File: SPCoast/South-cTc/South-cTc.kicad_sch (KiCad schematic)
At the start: 17 parts, among them SW783 783, SW795 795, SW799 799, U1 8, U2 9, U3 10

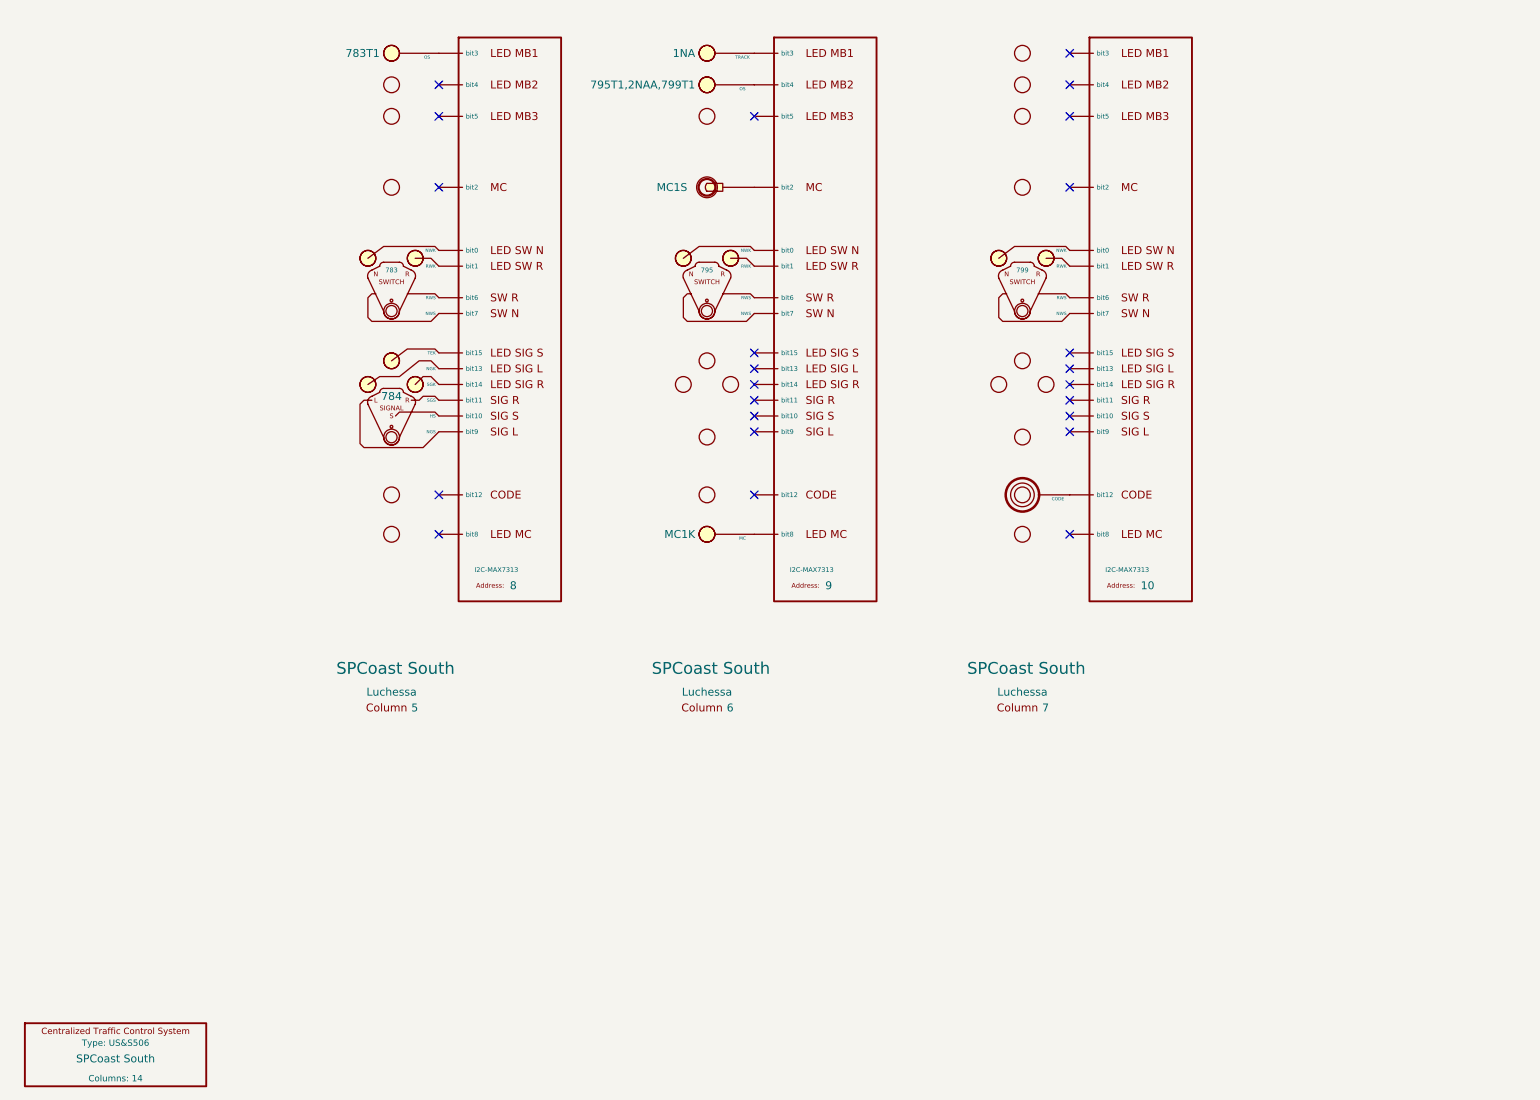
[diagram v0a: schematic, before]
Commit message: feat(kicad): restructure South-cTc into per-interlocking sheets with codelines
- Root sheet holds the CtcMachine; one hierarchical sheet per
  interlocking (Gilroy CalTrain, Gilroy Interchange, Luchessa,
  Christopher, Corporal, Sargent, Watsonville), each with a
  Codeline-VIRTUAL symbol carrying its Station.
- Luchessa sheet: columns 5-7 bind their appliances by column pins
  (membership from the netlist, not X alignment); appliances and drivers
  carry Role/Kind.
- Repair: root sheet UUID now matches the instance paths (kicad-cli
  exported zero nets before); .kicad_pro root filename case restored.
- Normalise Role/Kind values (MACHINE, COLUMN, APPLIANCE, IODRIVER;
  SWITCH_LEVER, SIGNAL_LEVER, LOCK_LEVER, LAMP, CODE, MAINTAINER_CALL),
  point stale PanelColumn_1/_2 copies back at the library symbol, and
  restore lamp IndicationTokens (783T1, 795T1,2NAA,799T1, 1NA, MC1K)
  lost to a library default.

Verified: kicad-cli netlist has 72 nets; ERC 0 violations; desk
playtest resolves every Luchessa appliance to one column and its
MAX7313 bits, matching examples/spcoast_ctc/IO-I2C.h.

Co-Authored-By: Claude Opus 5.5 (1M context) <noreply@anthropic.com>
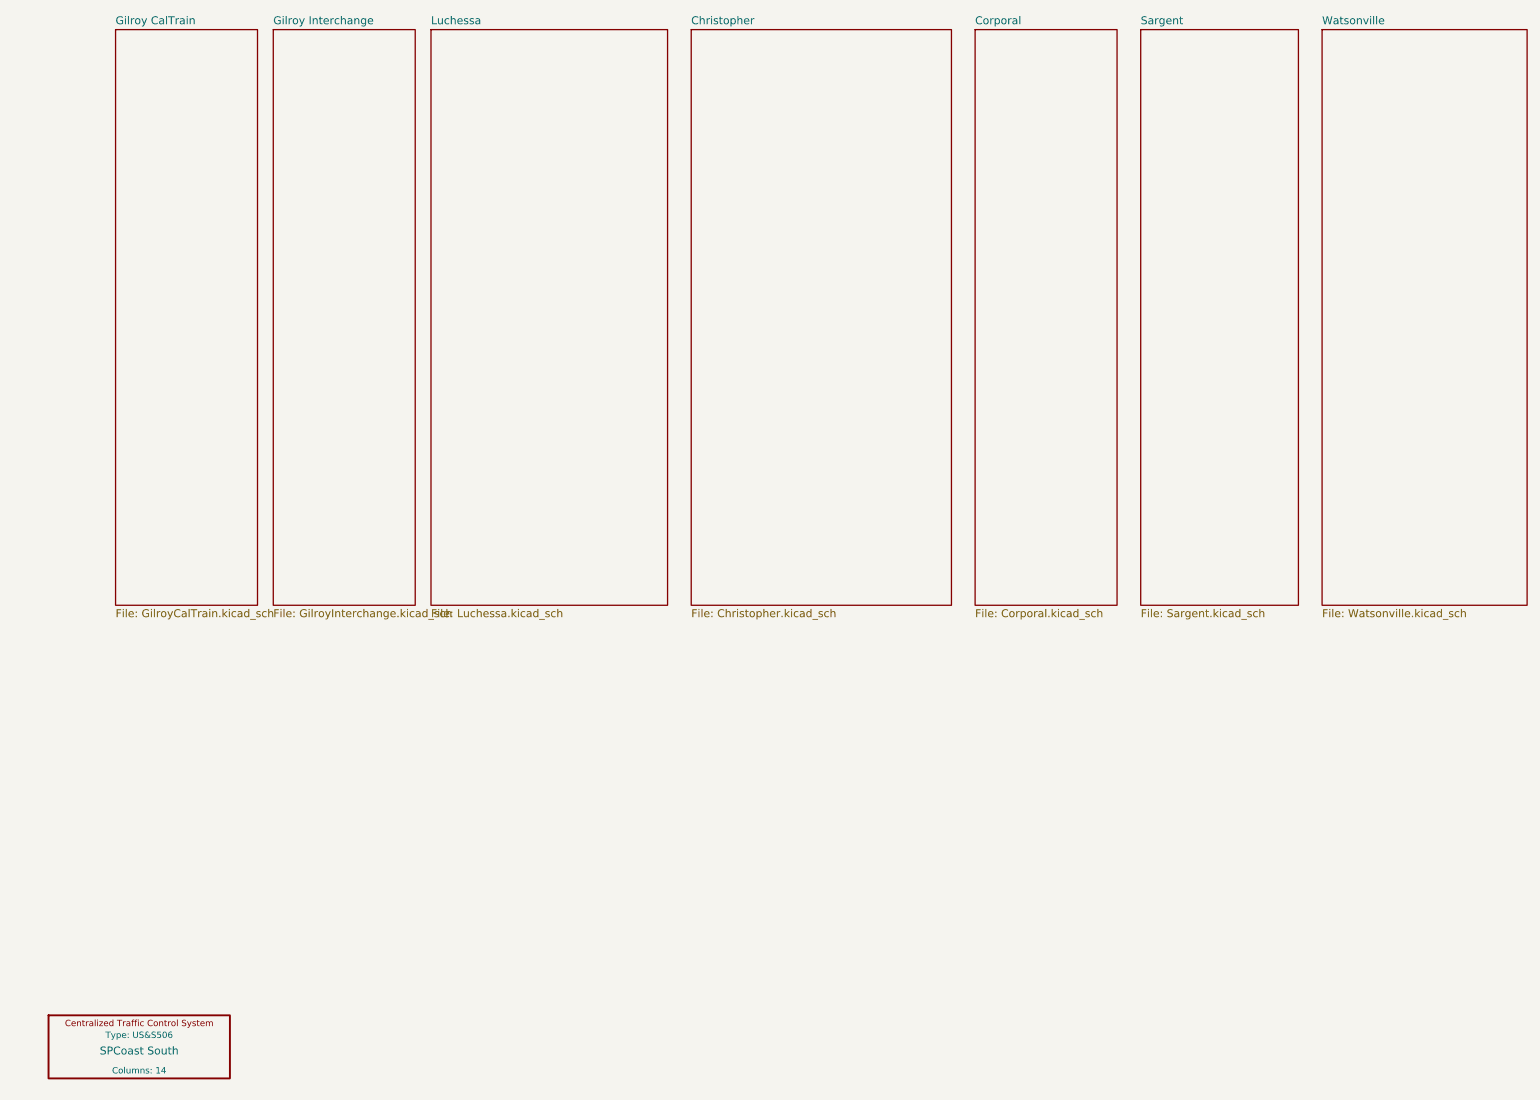
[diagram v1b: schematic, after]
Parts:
- removed AUX1: MC1, symbol RailroadPanel:PanelAuxiliary
- removed CODE1: CODE, symbol RailroadPanel:PanelCode
- removed COL1: 5, symbol RailroadPanel:PanelColumn
- removed COL2: 6, symbol RailroadPanel:PanelColumn
- removed COL3: 7, symbol RailroadPanel:PanelColumn
- removed LAMP1, LAMP2: OS, symbol RailroadPanel:PanelLamp-RED
- removed LAMP3: MC, symbol RailroadPanel:PanelLamp-YELLOW
- removed LAMP4: TRACK, symbol RailroadPanel:PanelLamp-YELLOW
- removed MACHINE1: SPCoast South, symbol RailroadPanel:CtcMachine
- removed SIG784: 784, symbol RailroadPanel:PanelSignal
- removed SW783: 783, symbol RailroadPanel:PanelSwitch
- removed SW795: 795, symbol RailroadPanel:PanelSwitch
- removed SW799: 799, symbol RailroadPanel:PanelSwitch
- removed U1: 8, symbol RailroadPanel:PanelColumn-MAX7313
- removed U2: 9, symbol RailroadPanel:PanelColumn-MAX7313
- removed U3: 10, symbol RailroadPanel:PanelColumn-MAX7313
- added MACHINE2: SPCoast South, symbol RailroadPanel:CtcMachine
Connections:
- no-connect marks 24 -> 0
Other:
- added sheet Christopher (Christopher.kicad_sch)
- added sheet Corporal (Corporal.kicad_sch)
- added sheet Gilroy CalTrain (GilroyCalTrain.kicad_sch)
- added sheet Gilroy Interchange (GilroyInterchange.kicad_sch)
- added sheet Luchessa (Luchessa.kicad_sch)
- added sheet Sargent (Sargent.kicad_sch)
- added sheet Watsonville (Watsonville.kicad_sch)
- company: SPCoast -> SPCoast Railroad
- title: SPCoast South cTc - Dispatcher Desk -> South cTc

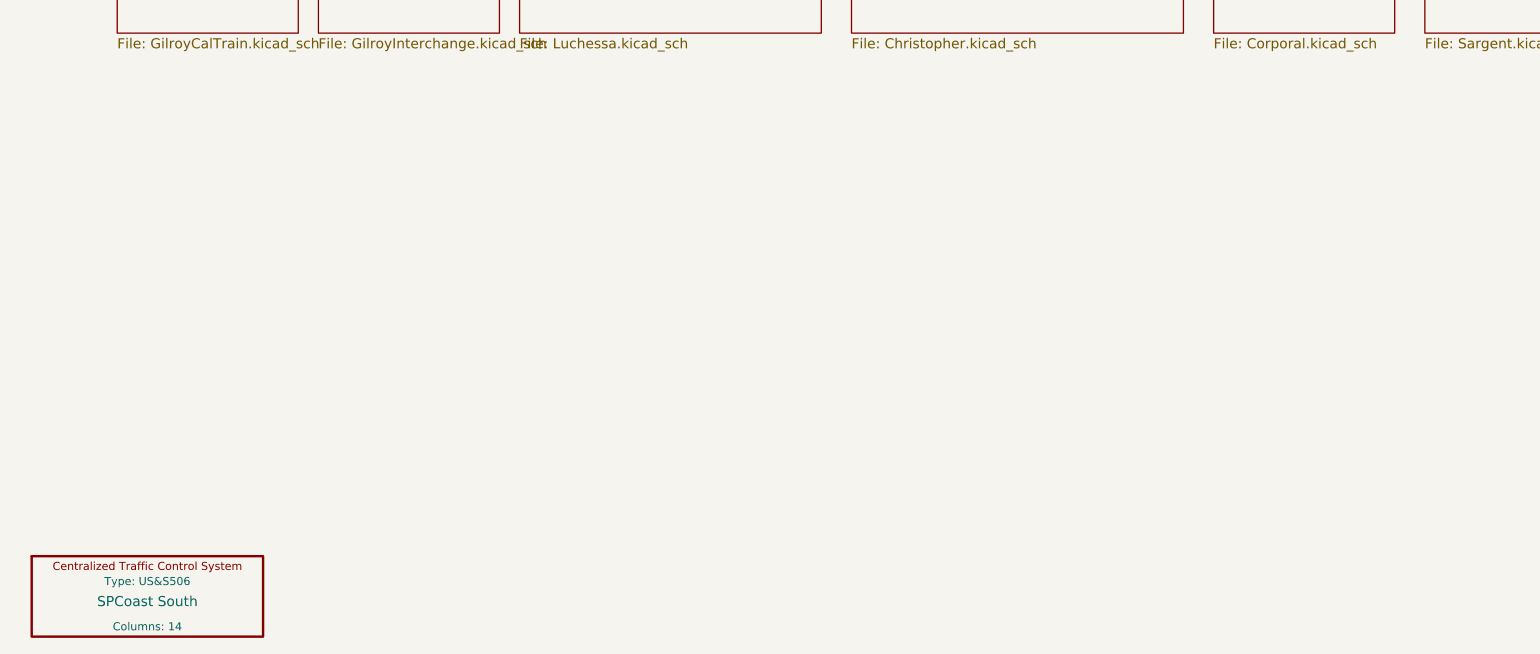
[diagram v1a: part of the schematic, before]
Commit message: SPCoast: derail pin R, track circuit names end in T, code line symbols on the root sheet
Working-tree changes from the 2026-10-01..03 vocabulary review with
FieldUnit-Subdivision (docs/adr/0001-code-line-type-contract.md):

- Switch_Powered_Derail pin 2 is R (through path = REVERSE) in the seven
  plant schematics (library Railroad.kicad_sym renamed alongside; not in git)
- Luchessa track circuits renamed to end in T (1SAT, 2NAAT, ...); MC1 moved
  to CP Gilroy's house
- South-cTc: transports (MQTT, TimeCode, CMRInet, Loconet) on the root
  sheet on the CtcMachine Transports pin; field stations as encoding
  instances on the Luchessa sheet; two Luchessa lamp tokens renamed
- Six plant projects (Christopher, Corporal, GilroyCalTrain,
  GilroyInterchange, Sargent, Watsonville) added as drawn so far; Watsonville
  updated 2026-10-02

Co-Authored-By: Claude Fable 5.1 <noreply@anthropic.com>
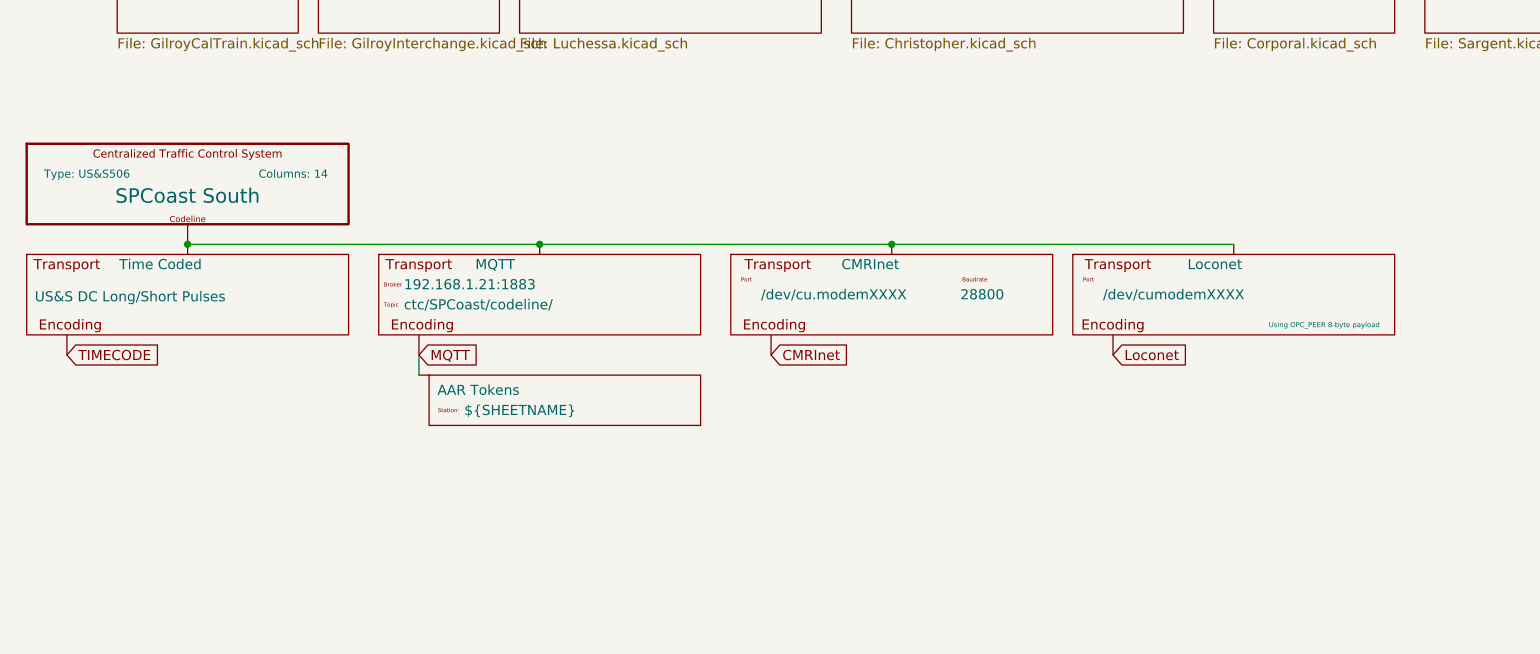
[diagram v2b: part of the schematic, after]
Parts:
- added Encoding1: AAR Tokens, symbol RailroadPanel:Codeline-Encoding-AAR
- added Transport5: Time Coded, symbol RailroadPanel:Codeline-Transport-TimeCode
- added Transport6: MQTT, symbol RailroadPanel:Codeline-Transport-MQTT
- added Transport7: CMRInet, symbol RailroadPanel:Codeline-Transport-CMRInet
- added Transport8: Loconet, symbol RailroadPanel:Codeline-Transport-Loconet
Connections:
- new net: MACHINE2.1 (Transports), Transport5.1 (Codeline), Transport6.1 (Codeline), Transport7.1 (Codeline), Transport8.1 (Codeline)
- new net CMRInet: Transport7.2 (Encoding)
- new net Loconet: Transport8.2 (Encoding)
- new net MQTT: Encoding1.1 (Encoding), Transport6.2 (Encoding)
- new net TIMECODE: Transport5.2 (Encoding)

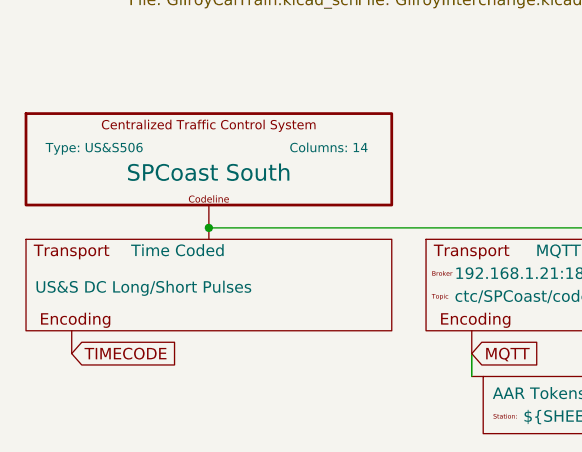
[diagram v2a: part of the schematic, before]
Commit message: SPCoast: owner's edits: schematics synced with the revised symbol libraries (baseline)
Update Symbols from Library on all plant and desk sheets; CP values for
Christopher, GilroyInterchange and Luchessa; Restricted Speed markers
consolidated in Corporal, Luchessa and Sargent.

Observed in the diff, not changed by the sweep that follows: CP changed on 23
symbols (Christopher: prefix removed, 815/815A/IND now Christopher North) and
added on 12 (GilroyInterchange); two lamps' Color reset to their symbol variant
(Christopher LMP93 red -> yellow, Sargent LMP133 yellow -> red).

Verified: netlists keep their net counts (Christopher 33, Corporal 26,
GilroyCalTrain 27, GilroyInterchange 22, Luchessa 34, Sargent 18, Watsonville
96, South-cTc 341); desk compiles to 75 appliances, 137 bindings, 14 columns;
no root-UUID regression.

Co-Authored-By: Claude Sonnet 5.5 <noreply@anthropic.com>
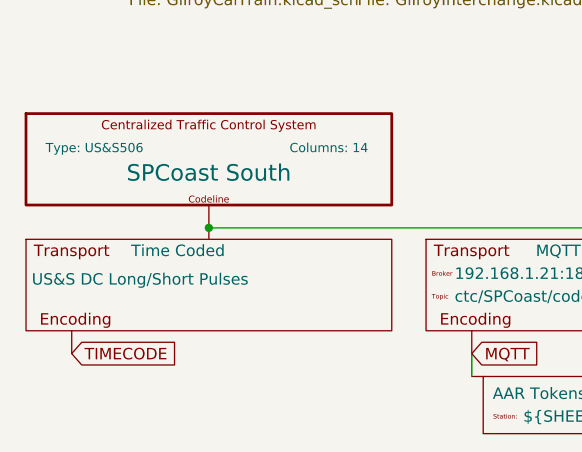
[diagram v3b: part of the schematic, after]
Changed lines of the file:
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@@
 			)
 		)
-		(property "Description" "One physical dispatcher cTc machine (protocol/vocabulary + desk geometry)."
+		(property "Description" "One physical dispatcher cTc machine (protocol/vocabulary)."
 			(at 48.895 147.955 0)
 			(hide yes)
@@
 		)
 		(property "Description" "US&S DC Long/Short Pulses"
-			(at 20.066 155.194 0)
+			(at 19.685 154.305 0)
 			(show_name no)
 			(do_not_autoplace yes)

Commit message: chore(kicad): masts and maintainer calls carry no CP; IRJ-Signals do; CMRInet Kind is CMRI
Owner decision: an IRJ-Signal is the single source of a signal's control point
(a mast attaches to exactly one IRJ-Signal through its SIGNAL pin); a
maintainer call is tied to its house by the netlist.
- CP dropped from 23 masts and 5 maintainer calls.
- 7 empty IRJ-Signal CPs filled with the plant's only house (Corporal, Sargent).
- 43 empty Name fields that KiCad re-added to Christopher dropped again.
- Codeline-Transport Kind CMRInet -> CMRI on the placed instance and the
  embedded library copy (South-cTc root sheet).

Verified: per-symbol before/after comparison shows only these changes; every
IRJ-Signal in all seven plants has a CP naming one of its plant's houses; net
counts unchanged (Christopher 33, Corporal 26, GilroyCalTrain 27,
GilroyInterchange 22, Luchessa 34, Sargent 18, Watsonville 96, South-cTc 341);
desk compiles to 75 appliances, 137 bindings, 14 columns. Remaining CP
diagnostic: Sargent's Corporal:2NAT placeholder (cross-plant reference).

Co-Authored-By: Claude Sonnet 5.5 <noreply@anthropic.com>
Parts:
- Transport7: Kind CMRInet -> CMRI
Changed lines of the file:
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@@
 			)
 		)
-		(property "Kind" "CMRInet"
+		(property "Kind" "CMRI"
 			(at 123.19 151.13 0)
 			(hide yes)

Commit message: SPCoast: owner's edit: CtcMachine carries Railroad = SPCoast (baseline)
Verified: South-cTc exports 341 nets and 677 components, unchanged.

Co-Authored-By: Claude Sonnet 5.5 <noreply@anthropic.com>
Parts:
- MACHINE2: Railroad (none) -> SPCoast
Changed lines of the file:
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@@
 		)
 		(property "Value" "SPCoast South"
-			(at 39.37 142.494 0)
+			(at 39.116 140.208 0)
 			(show_name no)
 			(do_not_autoplace yes)
@@
 		)
 		(property "Type" "US&S506"
-			(at 26.67 139.7 0)
-			(show_name yes)
+			(at 24.511 145.034 0)
+			(show_name no)
 			(do_not_autoplace yes)
 			(effects
 				(font
-					(size 1.016 1.016)
+					(size 0.762 0.762)
 				)
 			)
 		)
 		(property "Era" ""
-			(at 48.895 134.62 0)
+			(at 21.717 132.715 0)
 			(hide yes)
 			(show_name yes)
@@
 		)
 		(property "Role" "MACHINE"
-			(at 48.895 134.62 0)
+			(at 25.4 130.937 0)
 			(hide yes)
 			(show_name yes)
@@
 		)
 		(property "Columns" "14"
-			(at 52.705 139.7 0)
-			(show_name yes)
+			(at 33.401 145.034 0)
+			(show_name no)
 			(do_not_autoplace yes)
 			(effects
 				(font
-					(size 1.016 1.016)
+					(size 0.762 0.762)
 				)
 			)
 		)
+		(property "Railroad" "SPCoast"
+			(at 49.022 145.161 0)
+			(show_name no)
+			(do_not_autoplace yes)
+			(effects
+				(font
+					(size 0.762 0.762)
+				)
+				(justify left)
+			)
+		)

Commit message: SPCoast: owner's edits: 03T in 0101T, South-cTc sheet file renamed GilroyCaltrain.kicad_sch (baseline)
The rename changes only letter case, which git on a case-insensitive filesystem does not see; the index entry was replaced explicitly. The sheet name still contains a typo (Caltain), fixed next.

Co-Authored-By: Claude Sonnet 5.5 <noreply@anthropic.com>
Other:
- sheet Gilroy CalTrain renamed Gilroy Caltain
- sheet Gilroy Caltain: file GilroyCalTrain.kicad_sch -> GilroyCaltrain.kicad_sch
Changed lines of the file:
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@@
 			(color 0 0 0 0)
 		)
-		(property "Sheetname" "Gilroy CalTrain"
+		(property "Sheetname" "Gilroy Caltain"
 			(at 30.48 28.4984 0)
 			(show_name no)
@@
 			)
 		)
-		(property "Sheetfile" "GilroyCalTrain.kicad_sch"
+		(property "Sheetfile" "GilroyCaltrain.kicad_sch"
 			(at 30.48 122.5046 0)
 			(show_name no)

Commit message: fix(kicad): South-cTc sheet name typo Gilroy Caltain -> Gilroy Caltrain
Sheet name only (sheet names are not sources of truth); fixed in the root sheet and the sheets list of South-cTc.kicad_pro.

Verified: desk netlist 341 nets, 677 components; desk compiles to 75 appliances, 137 bindings, 14 columns.

Co-Authored-By: Claude Sonnet 5.5 <noreply@anthropic.com>
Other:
- sheet Gilroy Caltain renamed Gilroy Caltrain
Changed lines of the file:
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@@
 			(color 0 0 0 0)
 		)
-		(property "Sheetname" "Gilroy Caltain"
+		(property "Sheetname" "Gilroy Caltrain"
 			(at 30.48 28.4984 0)
 			(show_name no)
